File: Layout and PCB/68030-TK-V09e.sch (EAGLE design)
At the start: 75 parts, among them IC10 74HCT245DW, IC11 74HCT245DW, IC4 74HCT245DW, IC5 74HCT245DW, IC6 74HCT245DW, IC8 74HCT245DW, IC9 74HCT245DW, X1 FABC96R

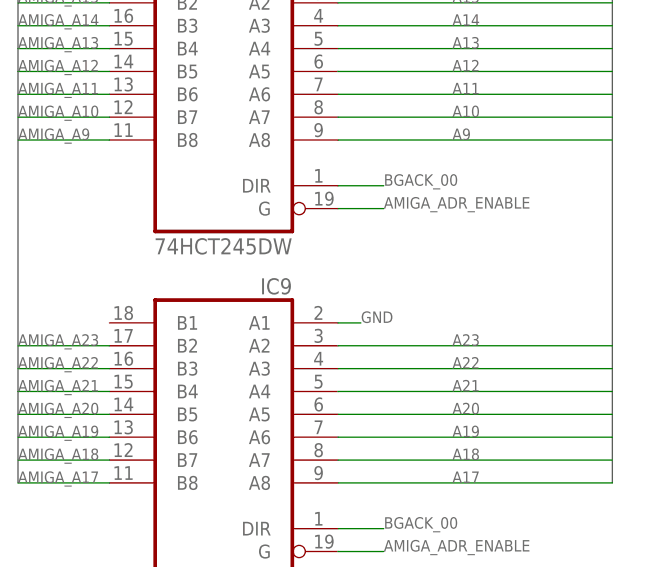
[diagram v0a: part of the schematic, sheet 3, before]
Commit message: Reset-Problem solved
The AMiga was not able to recover from a reste, because the e-clock was
not generated properly during reste.
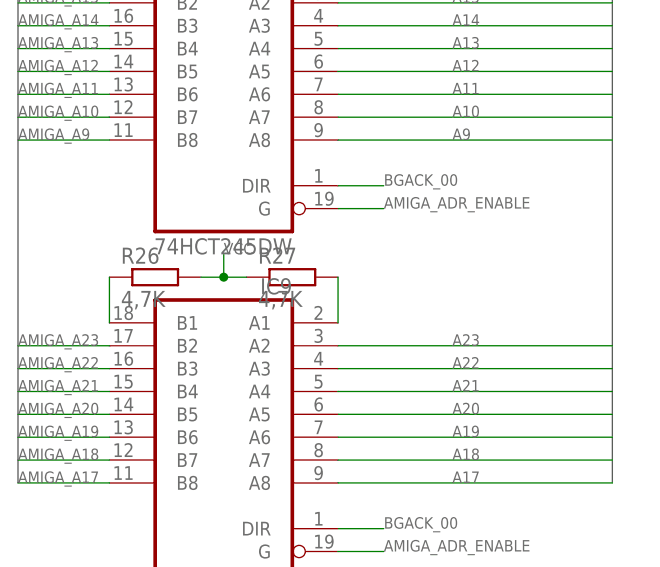
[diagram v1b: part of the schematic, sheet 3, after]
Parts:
- added R26, R27: 4,7K, rcl:R-EU_R0603
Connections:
- new net N$3: IC9A.B1, R26.1
- new net N$4: IC9A.A1, R27.2
- net GND: no longer IC9A.A1
- net VCC: now also R26.2, R27.1
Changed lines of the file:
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@@
 <part name="R24" library="rcl" deviceset="R-EU_" device="R0603" value="4,7k"/>
 <part name="R25" library="rcl" deviceset="R-EU_" device="R0603" value="4,7k"/>
+<part name="R26" library="rcl" deviceset="R-EU_" device="R0603" value="4,7K"/>
+<part name="R27" library="rcl" deviceset="R-EU_" device="R0603" value="4,7K"/>
 </parts>
 <sheets>
@@
 <instance part="RN8" gate="C" x="96.52" y="157.48"/>
 <instance part="RN8" gate="D" x="96.52" y="152.4"/>
+<instance part="R26" gate="G$1" x="20.32" y="91.44"/>
+<instance part="R27" gate="G$1" x="35.56" y="91.44"/>
 </instances>
 <busses>
@@
 <junction x="101.6" y="162.56"/>
 </segment>
-<segment>
-<pinref part="IC9" gate="A" pin="A1"/>
-<wire x1="40.64" y1="86.36" x2="43.18" y2="86.36" width="0.1524" layer="91"/>
-<label x="43.18" y="86.36" size="1.27" layer="95"/>
-</segment>
 </net>
 <net name="VCC" class="0">
@@
 <junction x="208.28" y="124.46"/>
 </segment>
+<segment>
+<pinref part="R26" gate="G$1" pin="2"/>
+<pinref part="R27" gate="G$1" pin="1"/>
+<wire x1="25.4" y1="91.44" x2="27.94" y2="91.44" width="0.1524" layer="91"/>
+<wire x1="27.94" y1="91.44" x2="30.48" y2="91.44" width="0.1524" layer="91"/>
+<wire x1="27.94" y1="91.44" x2="27.94" y2="93.98" width="0.1524" layer="91"/>
+<junction x="27.94" y="91.44"/>
+<label x="27.94" y="93.98" size="1.27" layer="95"/>
+</segment>
 </net>
 <net name="AMIGA_BUS_ENABLE_HIGH" class="0">
@@
 </segment>
 </net>
+<net name="N$3" class="0">
+<segment>
+<pinref part="IC9" gate="A" pin="B1"/>
+<pinref part="R26" gate="G$1" pin="1"/>
+<wire x1="15.24" y1="86.36" x2="15.24" y2="91.44" width="0.1524" layer="91"/>
+</segment>
+</net>
+<net name="N$4" class="0">
+<segment>
+<pinref part="R27" gate="G$1" pin="2"/>
+<pinref part="IC9" gate="A" pin="A1"/>
+<wire x1="40.64" y1="91.44" x2="40.64" y2="86.36" width="0.1524" layer="91"/>
+</segment>
+</net>
